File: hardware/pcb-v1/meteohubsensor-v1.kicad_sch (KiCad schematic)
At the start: 18 parts, among them J1 BAT, J2 BMP280, J3 DHT22, J4 ANEMO, J5 PLUVIO, J6 GIROUETTE, U1 ESP32-S3 Super Mini N4R2, U2 Module 3V3 Youmi

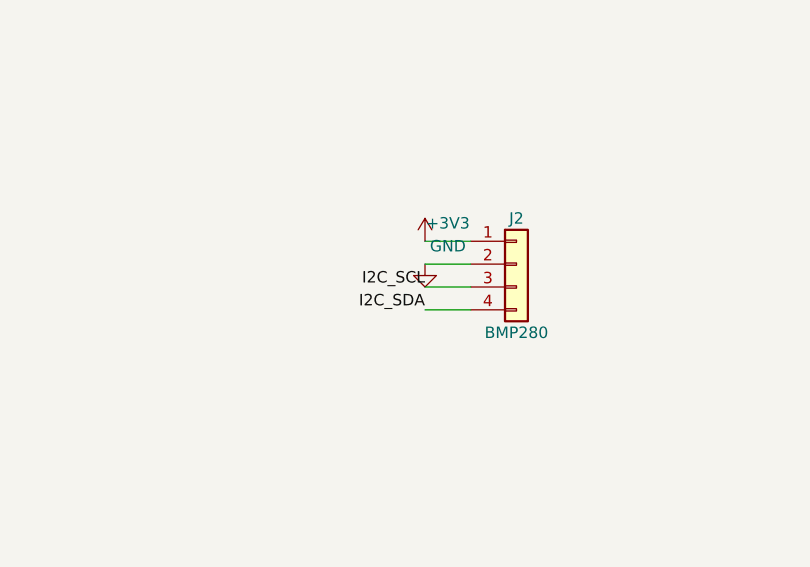
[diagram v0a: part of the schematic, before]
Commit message: Update 3D model and footprint for Regulator Module 3V3; add BOM documentation
- Modified the 3D shape of the Regulator Module 3V3 to adjust dimensions and colors.
- Updated the KiCad footprint for the Regulator Module 3V3, correcting pad positions and descriptions.
- Added a comprehensive Bill of Materials (BOM) for the MeteoHubSensor v1, detailing components, quantities, and specifications.
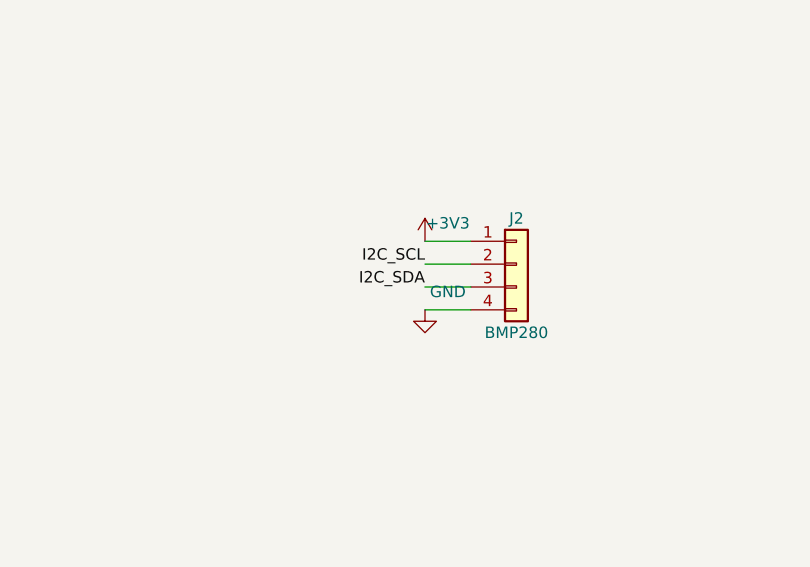
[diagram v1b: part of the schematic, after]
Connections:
- net GND: now also J2.4 (Pin_4); no longer J2.2 (Pin_2)
- net I2C_SCL: now also J2.2 (Pin_2); no longer J2.3 (Pin_3)
- net I2C_SDA: now also J2.3 (Pin_3); no longer J2.4 (Pin_4)
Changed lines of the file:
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@@
 	)
 	(label "I2C_SCL"
+		(at 320.04 55.88 180)
+		(effects
+			(font
+				(size 1.27 1.27)
+			)
+			(justify right bottom)
+		)
+	)
+	(label "I2C_SDA"
 		(at 320.04 58.42 180)
-		(effects
-			(font
-				(size 1.27 1.27)
-			)
-			(justify right bottom)
-		)
-	)
-	(label "I2C_SDA"
-		(at 320.04 60.96 180)
 		(effects
 			(font
@@
 	(symbol
 		(lib_id "power:GND")
-		(at 320.04 55.88 0)
+		(at 320.04 60.96 0)
 		(unit 1)
 		(body_style 1)
@@
 		(dnp no)
 		(property "Reference" "#PWR10"
-			(at 322.58000000000004 55.88 0)
+			(at 322.58000000000004 60.96 0)
 			(hide yes)
 			(effects
@@
 		)
 		(property "Value" "GND"
-			(at 322.58000000000004 53.88 0)
+			(at 322.58000000000004 58.96 0)
 			(effects
 				(font
@@
 		)
 		(property "Footprint" ""
-			(at 320.04 55.88 0)
-			(hide yes)
-			(effects
-				(font
-					(size 1.27 1.27)
-				)
-			)
-		)
-		(property "Datasheet" ""
-			(at 320.04 55.88 0)
-			(hide yes)
-			(effects
+			(at 320.04 60.96 0)
+			(hide yes)
+			(effects
+				(font
+					(size 1.27 1.27)
+				)
+			)
+		)
+		(property "Datasheet" ""
+			(at 320.04 60.96 0)
+			(hide yes)
+			(effects
